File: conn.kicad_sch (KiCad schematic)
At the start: 59 parts, among them J10 MicroFit_2x04, J11 JST_1x04, J12 MicroFit_2x04, J13 JST_01x02, J14 JST_1x02, J15 JST_1x02_P, J16 MLX_1x03, J17 MLX_1x03, J5 JST_B6B-XH, J6 JST_1x04, J7 MicroFit_2x04, J8 JST_1x04, J9 JST_1x04, SW2 !EMERG STOP!

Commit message: Much to do about power
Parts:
- NT10, NT11, NT12, NT13, NT14, NT15, NT16, NT17, NT18, NT19, NT2, NT20, NT21, NT24, NT25, NT3, NT4, NT5, NT7, NT8, NT9: footprint -ProjectNetTie-2_SMD_Pad0.3mm -> -Project:NetTie-2_SMD_Pad0.3mm
- NT22, NT23, NT6: footprint -ProjectNetTie-2_SMD_Pad1.0mm -> -Project:NetTie-2_SMD_Pad1.0mm
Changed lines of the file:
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@@
       (effects (font (size 1.27 1.27)) hide)
     )
-    (property "Footprint" "-ProjectNetTie-2_SMD_Pad0.3mm" (id 2) (at 146.05 100.33 0)
+    (property "Footprint" "-Project:NetTie-2_SMD_Pad0.3mm" (id 2) (at 146.05 100.33 0)
       (effects (font (size 1.27 1.27)) hide)
     )
@@
       (effects (font (size 1.27 1.27)) hide)
     )
-    (property "Footprint" "-ProjectNetTie-2_SMD_Pad0.3mm" (id 2) (at 50.8 172.72 0)
+    (property "Footprint" "-Project:NetTie-2_SMD_Pad0.3mm" (id 2) (at 50.8 172.72 0)
       (effects (font (size 1.27 1.27)) hide)
     )
@@
       (effects (font (size 1.27 1.27)) hide)
     )
-    (property "Footprint" "-ProjectNetTie-2_SMD_Pad0.3mm" (id 2) (at 61.595 51.435 0)
+    (property "Footprint" "-Project:NetTie-2_SMD_Pad0.3mm" (id 2) (at 61.595 51.435 0)
       (effects (font (size 1.27 1.27)) hide)
     )
@@
       (effects (font (size 1.27 1.27)) hide)
     )
-    (property "Footprint" "-ProjectNetTie-2_SMD_Pad0.3mm" (id 2) (at 50.8 170.18 0)
+    (property "Footprint" "-Project:NetTie-2_SMD_Pad0.3mm" (id 2) (at 50.8 170.18 0)
       (effects (font (size 1.27 1.27)) hide)
     )
@@
       (effects (font (size 1.27 1.27)) hide)
     )
-    (property "Footprint" "-ProjectNetTie-2_SMD_Pad1.0mm" (id 2) (at 118.11 76.2 0)
+    (property "Footprint" "-Project:NetTie-2_SMD_Pad1.0mm" (id 2) (at 118.11 76.2 0)
       (effects (font (size 1.27 1.27)) hide)
     )
@@
       (effects (font (size 1.27 1.27)) hide)
     )
-    (property "Footprint" "-ProjectNetTie-2_SMD_Pad0.3mm" (id 2) (at 61.595 77.47 0)
+    (property "Footprint" "-Project:NetTie-2_SMD_Pad0.3mm" (id 2) (at 61.595 77.47 0)
       (effects (font (size 1.27 1.27)) hide)
     )
@@
       (effects (font (size 1.27 1.27)) hide)
     )
-    (property "Footprint" "-ProjectNetTie-2_SMD_Pad0.3mm" (id 2) (at 61.595 85.09 0)
+    (property "Footprint" "-Project:NetTie-2_SMD_Pad0.3mm" (id 2) (at 61.595 85.09 0)
       (effects (font (size 1.27 1.27)) hide)
     )
@@
       (effects (font (size 1.27 1.27)) hide)
     )
-    (property "Footprint" "-ProjectNetTie-2_SMD_Pad0.3mm" (id 2) (at 50.8 167.64 0)
+    (property "Footprint" "-Project:NetTie-2_SMD_Pad0.3mm" (id 2) (at 50.8 167.64 0)
       (effects (font (size 1.27 1.27)) hide)
     )
@@
       (effects (font (size 1.27 1.27)) hide)
     )
-    (property "Footprint" "-ProjectNetTie-2_SMD_Pad0.3mm" (id 2) (at 50.8 165.1 0)
+    (property "Footprint" "-Project:NetTie-2_SMD_Pad0.3mm" (id 2) (at 50.8 165.1 0)
       (effects (font (size 1.27 1.27)) hide)
     )
@@
       (effects (font (size 1.27 1.27)) hide)
     )
-    (property "Footprint" "-ProjectNetTie-2_SMD_Pad0.3mm" (id 2) (at 61.595 92.71 0)
+    (property "Footprint" "-Project:NetTie-2_SMD_Pad0.3mm" (id 2) (at 61.595 92.71 0)
       (effects (font (size 1.27 1.27)) hide)
     )
@@
       (effects (font (size 1.27 1.27)) hide)
     )
-    (property "Footprint" "-ProjectNetTie-2_SMD_Pad1.0mm" (id 2) (at 60.96 153.67 0)
+    (property "Footprint" "-Project:NetTie-2_SMD_Pad1.0mm" (id 2) (at 60.96 153.67 0)
       (effects (font (size 1.27 1.27)) hide)
     )
@@
       (effects (font (size 1.27 1.27)) hide)
     )
-    (property "Footprint" "-ProjectNetTie-2_SMD_Pad0.3mm" (id 2) (at 61.595 87.63 0)
+    (property "Footprint" "-Project:NetTie-2_SMD_Pad0.3mm" (id 2) (at 61.595 87.63 0)
       (effects (font (size 1.27 1.27)) hide)
     )
@@
       (effects (font (size 1.27 1.27)) hide)
     )
-    (property "Footprint" "-ProjectNetTie-2_SMD_Pad0.3mm" (id 2) (at 61.595 80.01 0)
+    (property "Footprint" "-Project:NetTie-2_SMD_Pad0.3mm" (id 2) (at 61.595 80.01 0)
       (effects (font (size 1.27 1.27)) hide)
     )
@@
       (effects (font (size 1.27 1.27)) hide)
     )
-    (property "Footprint" "-ProjectNetTie-2_SMD_Pad0.3mm" (id 2) (at 61.595 90.17 0)
+    (property "Footprint" "-Project:NetTie-2_SMD_Pad0.3mm" (id 2) (at 61.595 90.17 0)
       (effects (font (size 1.27 1.27)) hide)
     )
@@
       (effects (font (size 1.27 1.27)) hide)
     )
-    (property "Footprint" "-ProjectNetTie-2_SMD_Pad0.3mm" (id 2) (at 61.595 59.055 0)
+    (property "Footprint" "-Project:NetTie-2_SMD_Pad0.3mm" (id 2) (at 61.595 59.055 0)
       (effects (font (size 1.27 1.27)) hide)
     )
@@
       (effects (font (size 1.27 1.27)) hide)
     )
-    (property "Footprint" "-ProjectNetTie-2_SMD_Pad0.3mm" (id 2) (at 146.05 102.87 0)
+    (property "Footprint" "-Project:NetTie-2_SMD_Pad0.3mm" (id 2) (at 146.05 102.87 0)
       (effects (font (size 1.27 1.27)) hide)
     )
@@
       (effects (font (size 1.27 1.27)) hide)
     )
-    (property "Footprint" "-ProjectNetTie-2_SMD_Pad0.3mm" (id 2) (at 61.595 53.975 0)
+    (property "Footprint" "-Project:NetTie-2_SMD_Pad0.3mm" (id 2) (at 61.595 53.975 0)
       (effects (font (size 1.27 1.27)) hide)
     )
@@
       (effects (font (size 1.27 1.27)) hide)
     )
-    (property "Footprint" "-ProjectNetTie-2_SMD_Pad1.0mm" (id 2) (at 116.84 35.56 0)
+    (property "Footprint" "-Project:NetTie-2_SMD_Pad1.0mm" (id 2) (at 116.84 35.56 0)
       (effects (font (size 1.27 1.27)) hide)
     )
@@
       (effects (font (size 1.27 1.27)) hide)
     )
-    (property "Footprint" "-ProjectNetTie-2_SMD_Pad0.3mm" (id 2) (at 61.595 107.95 0)
+    (property "Footprint" "-Project:NetTie-2_SMD_Pad0.3mm" (id 2) (at 61.595 107.95 0)
       (effects (font (size 1.27 1.27)) hide)
     )
@@
       (effects (font (size 1.27 1.27)) hide)
     )
-    (property "Footprint" "-ProjectNetTie-2_SMD_Pad0.3mm" (id 2) (at 61.595 113.03 0)
+    (property "Footprint" "-Project:NetTie-2_SMD_Pad0.3mm" (id 2) (at 61.595 113.03 0)
       (effects (font (size 1.27 1.27)) hide)
     )
@@
       (effects (font (size 1.27 1.27)) hide)
     )
-    (property "Footprint" "-ProjectNetTie-2_SMD_Pad0.3mm" (id 2) (at 61.595 110.49 0)
+    (property "Footprint" "-Project:NetTie-2_SMD_Pad0.3mm" (id 2) (at 61.595 110.49 0)
       (effects (font (size 1.27 1.27)) hide)
     )
@@
       (effects (font (size 1.27 1.27)) hide)
     )
-    (property "Footprint" "-ProjectNetTie-2_SMD_Pad0.3mm" (id 2) (at 61.595 56.515 0)
+    (property "Footprint" "-Project:NetTie-2_SMD_Pad0.3mm" (id 2) (at 61.595 56.515 0)
       (effects (font (size 1.27 1.27)) hide)
     )
@@
       (effects (font (size 1.27 1.27)) hide)
     )
-    (property "Footprint" "-ProjectNetTie-2_SMD_Pad0.3mm" (id 2) (at 61.595 61.595 0)
+    (property "Footprint" "-Project:NetTie-2_SMD_Pad0.3mm" (id 2) (at 61.595 61.595 0)
       (effects (font (size 1.27 1.27)) hide)
     )
@@
       (effects (font (size 1.27 1.27)) hide)
     )
-    (property "Footprint" "-ProjectNetTie-2_SMD_Pad0.3mm" (id 2) (at 61.595 82.55 0)
-      (effects (font (size 1.27 1.27)) hide)
-    )
+    (property "Footprint" "-Project:NetTie-2_SMD_Pad0.3mm" (id 2) (at 61.595 82.55 0)
+      (effects (font (size 1.27 1.27)) hide)
+    )

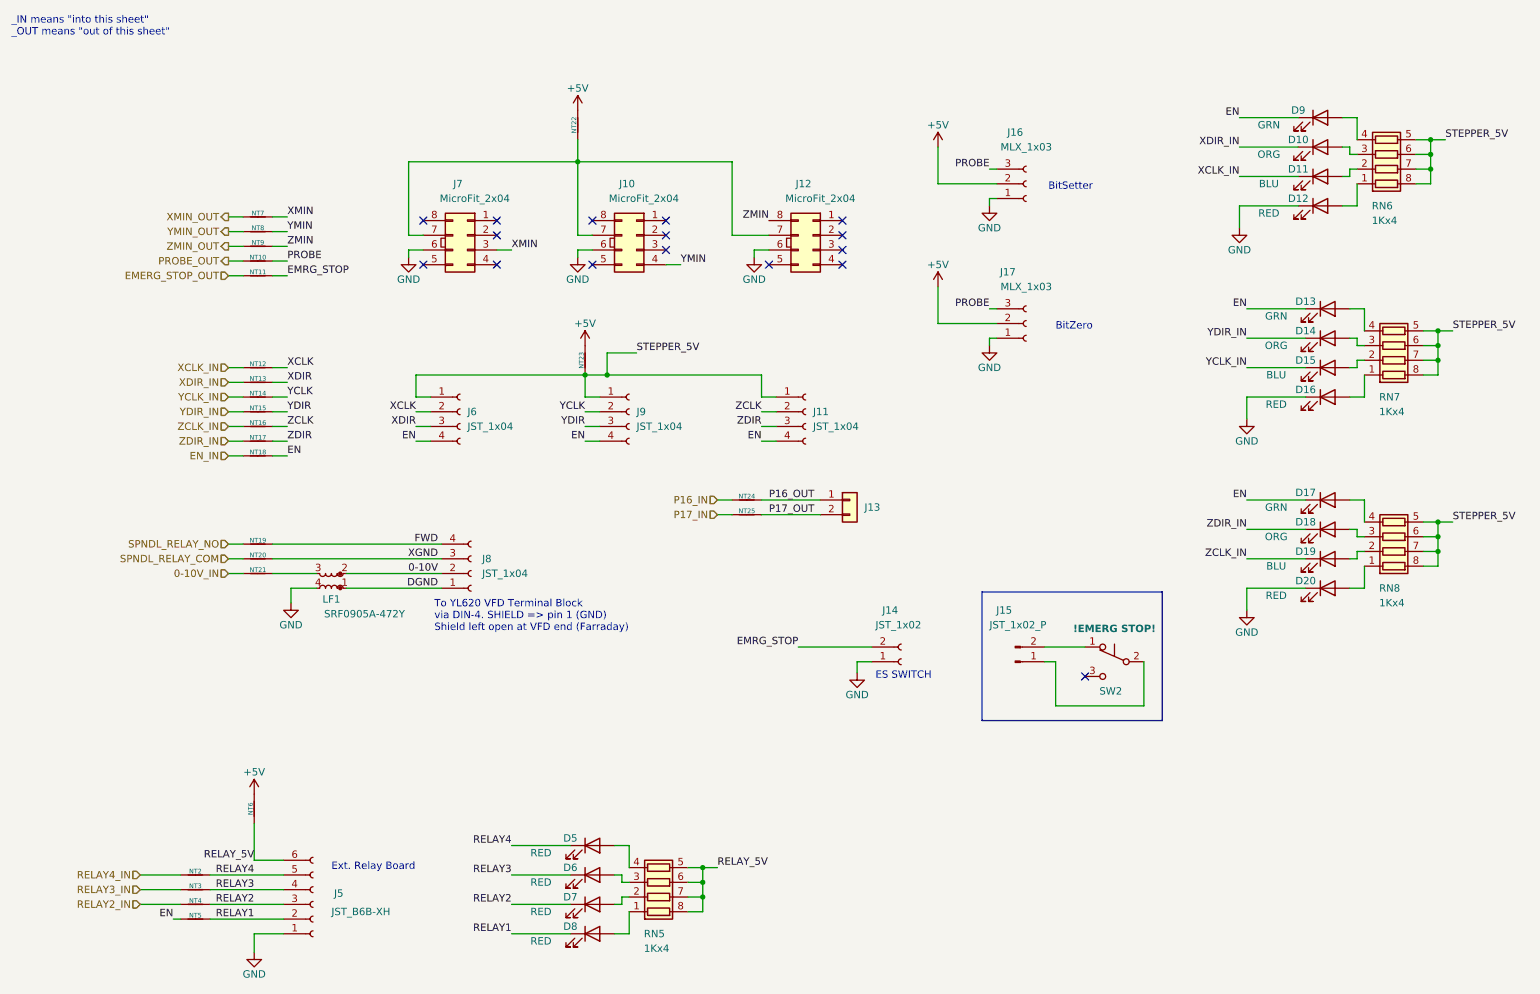
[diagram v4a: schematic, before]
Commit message: Routed power switching changes.
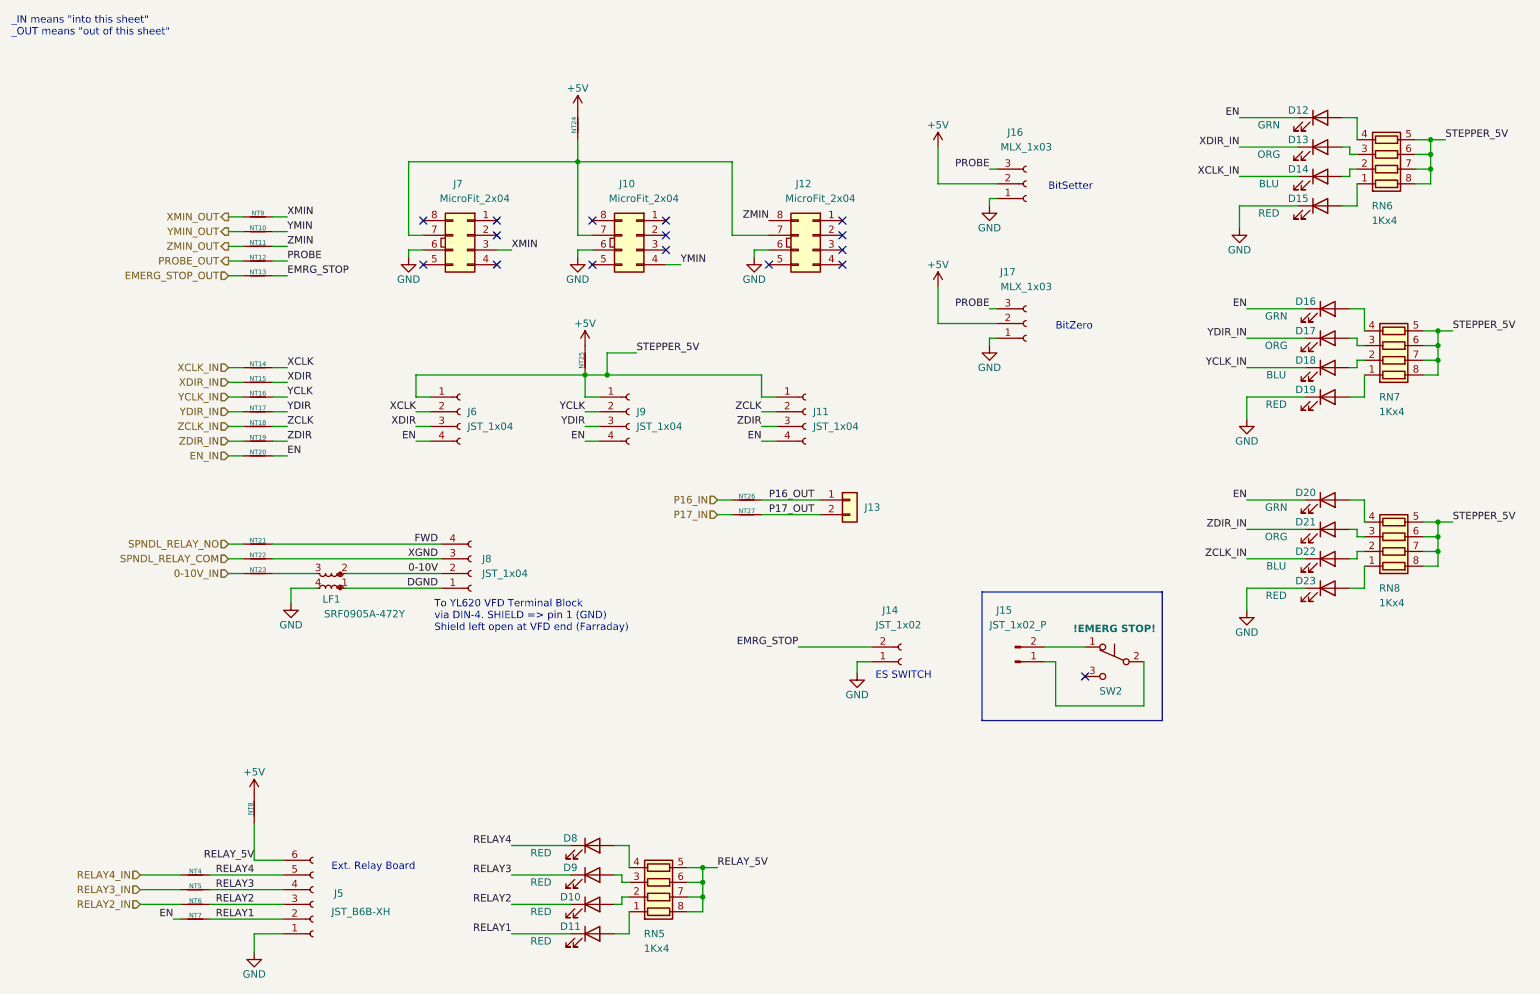
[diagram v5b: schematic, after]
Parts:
- renumbered D7 to D10, D8 to D11, D9 to D12, D10 to D13, D11 to D14, D12 to D15, D13 to D16, D14 to D17, D15 to D18, D16 to D19, D17 to D20, D18 to D21, D19 to D22, D20 to D23, D5 to D8, D6 to D9, NT8 to NT10, NT9 to NT11, NT10 to NT12, NT11 to NT13, NT12 to NT14, NT13 to NT15, NT14 to NT16, NT15 to NT17, NT16 to NT18, NT17 to NT19, NT18 to NT20, NT19 to NT21, NT20 to NT22, NT21 to NT23, NT22 to NT24, NT23 to NT25, NT24 to NT26, NT25 to NT27, NT2 to NT4, NT3 to NT5, NT4 to NT6, NT5 to NT7, NT6 to NT8, NT7 to NT9

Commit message: Tweaks and JLCPCB LCSC field name changes.
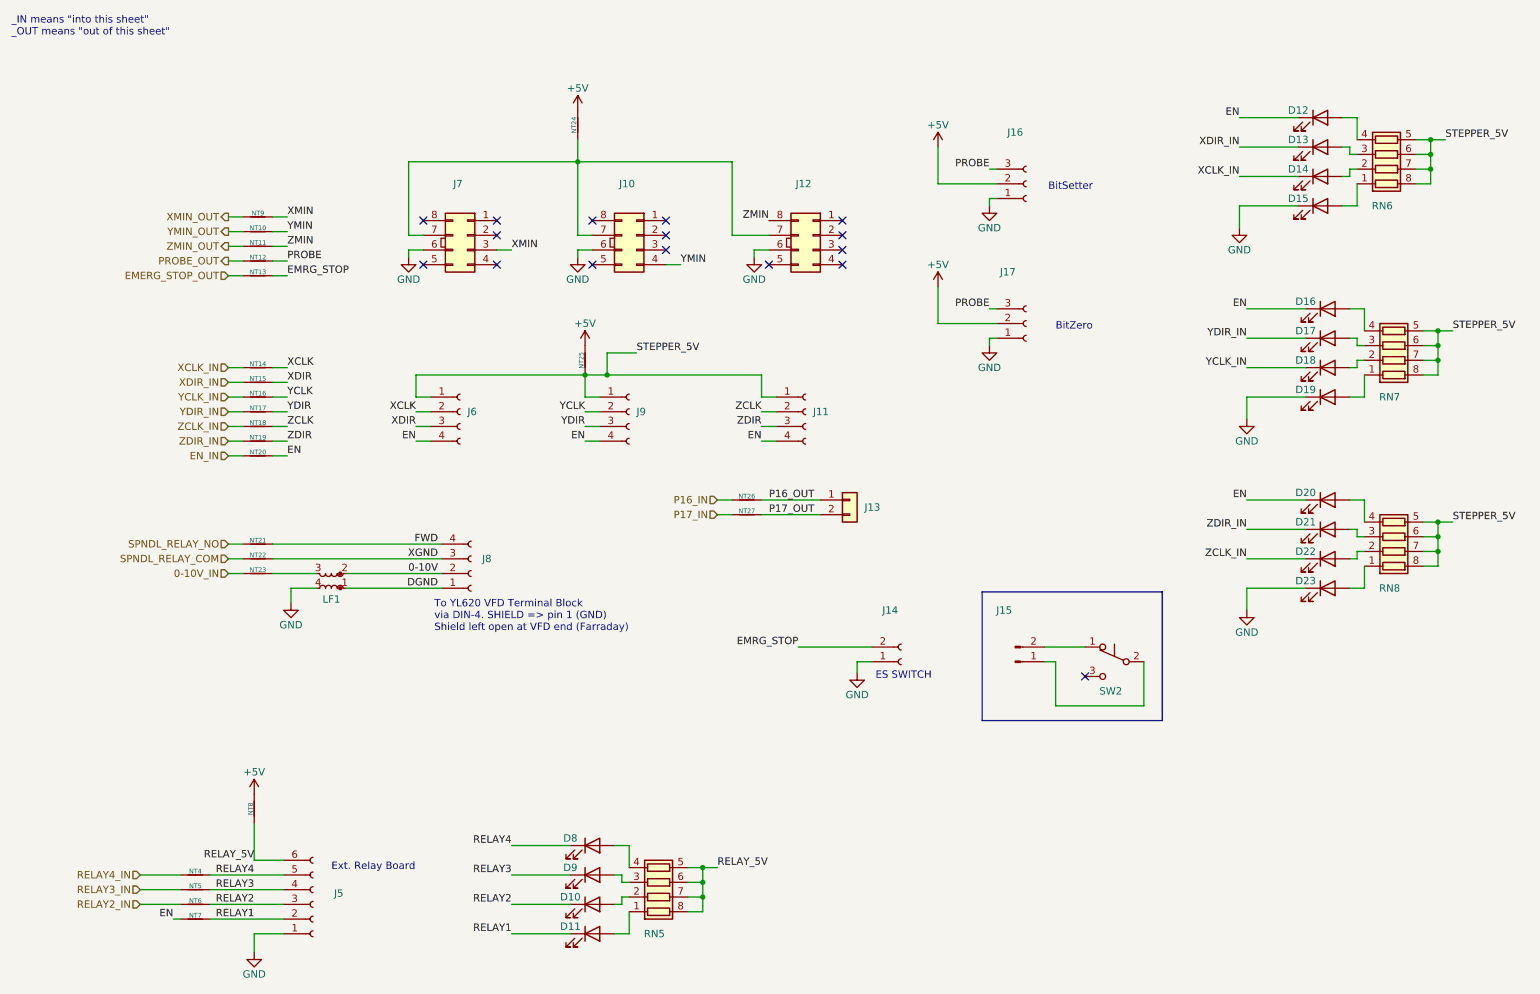
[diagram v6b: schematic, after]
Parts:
- D10, D11, D15, D19, D23, D8, D9: value RED -> (none); footprint LED_SMD:LED_0402_1005Metric -> (none)
- D12, D16, D20: value GRN -> (none); footprint LED_SMD:LED_0402_1005Metric -> (none)
- D13, D17, D21: value ORG -> (none); footprint LED_SMD:LED_0402_1005Metric -> (none)
- D14, D18, D22: value BLU -> (none); footprint LED_SMD:LED_0402_1005Metric -> (none)
- J10, J12, J7: value MicroFit_2x04 -> (none); footprint Connector_Molex:Molex_Micro-Fit_3.0_43045-0812_2x04_P3.00mm_Vertical -> (none)
- J11, J6, J8, J9: value JST_1x04 -> (none); footprint Connector_JST:JST_EH_S4B-EH_1x04_P2.50mm_Horizontal -> (none)
- J13: value JST_01x02 -> (none); footprint Connector_JST:JST_EH_B2B-EH-A_1x02_P2.50mm_Vertical -> (none); JLCMFR# B2B-XH-AM(LF)(SN) -> (none); JLCPART C161869 -> (none); LCSC (none) -> C161869; LCSCMFR# (none) -> B2B-XH-AM(LF)(SN)
- J14: value JST_1x02 -> (none); footprint Connector_JST:JST_EH_S2B-EH_1x02_P2.50mm_Horizontal -> (none); JLCPART C163035 -> (none); LCSC (none) -> C163035
- J15: value JST_1x02_P -> (none)
- J16, J17: value MLX_1x03 -> (none); footprint Connector_Molex:Molex_KK-254_AE-6410-03A_1x03_P2.54mm_Vertical -> (none)
- J5: value JST_B6B-XH -> (none); footprint Connector_JST:JST_EH_S6B-EH_1x06_P2.50mm_Horizontal -> (none)
- LF1: value SRF0905A-472Y -> (none); footprint Filter:Filter_Bourns_SRF0905_6.0x9.2mm -> (none)
- NT10, NT11, NT12, NT13, NT14, NT15, NT16, NT17, NT18, NT19, NT20, NT21, NT22, NT23, NT26, NT27, NT4, NT5, NT6, NT7, NT9: value DNI -> (none); footprint -Project:NetTie-2_SMD_Pad0.3mm -> (none)
- NT24, NT25, NT8: value DNI -> (none); footprint -Project:NetTie-2_SMD_Pad1.0mm -> (none)
- RN5, RN6, RN7, RN8: value 1Kx4 -> (none); footprint Resistor_SMD:R_Array_Convex_4x0603 -> (none); JLCMFR# 4D03WGJ0102T5E -> (none); JLCPART C20197 -> (none); LCSC (none) -> C20197; LCSCMFR# (none) -> 4D03WGJ0102T5E
- SW2: value !EMERG STOP! -> (none)
